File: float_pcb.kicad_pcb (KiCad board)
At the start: 4 copper layers, 64 x 64 mm, 77 parts, among them J1 Switch, J2 Conn_01x04, J3 USB_C, J4 Conn_01x03, J5 I2C, J6 Light, J7 Batt, J9 I2C, Q1 AO3400A, Q2 AO3400A, U1 TPSM863252, U2 TPSM863252, U3 USBLC6-2SC6, U4 ESP32-S3-WROOM-1, U5 USBLC6-4SC6, U6 USBLC6-4SC6

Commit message: More progress on V4
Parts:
- U4: value ESP32-S3-WROOM-1 -> ESP32-S3-WROOM-1U
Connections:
- net /VBUS renamed VBUS_USB
- net Net-(J3-D+-PadA6) renamed USBC_D+
- net Net-(J3-D--PadA7) renamed USBC_D-
- net Net-(U4-USB_D+) renamed ESP32_D+
- net Net-(U4-USB_D-) renamed ESP32_D-
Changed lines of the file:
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@@
 			)
 		)
-		(property "Value" "ESP32-S3-WROOM-1"
+		(property "Value" "ESP32-S3-WROOM-1U"
 			(at 0 2.46 0)
 			(unlocked yes)
@@
 			(size 1.5 0.9)
 			(layers "F.Cu" "F.Mask" "F.Paste")
-			(net "Net-(U4-USB_D-)")
+			(net "ESP32_D-")
 			(pinfunction "USB_D-_13")
 			(pintype "bidirectional")
@@
 			(size 1.5 0.9)
 			(layers "F.Cu" "F.Mask" "F.Paste")
-			(net "Net-(U4-USB_D+)")
+			(net "ESP32_D+")
 			(pinfunction "USB_D+_14")
 			(pintype "bidirectional")
@@
 			(layers "F.Cu" "F.Mask" "F.Paste")
 			(roundrect_rratio 0.25)
-			(net "/VBUS")
+			(net "VBUS_USB")
 			(pinfunction "VBUS_A4")
 			(pintype "passive")
@@
 			(layers "F.Cu" "F.Mask" "F.Paste")
 			(roundrect_rratio 0.25)
-			(net "Net-(J3-D+-PadA6)")
+			(net "USBC_D+")
 			(pinfunction "D+_A6")
 			(pintype "bidirectional")
@@
 			(layers "F.Cu" "F.Mask" "F.Paste")
 			(roundrect_rratio 0.25)
-			(net "Net-(J3-D--PadA7)")
+			(net "USBC_D-")
 			(pinfunction "D-_A7")
 			(pintype "bidirectional")
@@
 			(layers "F.Cu" "F.Mask" "F.Paste")
 			(roundrect_rratio 0.25)
-			(net "/VBUS")
+			(net "VBUS_USB")
 			(pinfunction "VBUS_A9")
 			(pintype "passive")
@@
 			(layers "F.Cu" "F.Mask" "F.Paste")
 			(roundrect_rratio 0.25)
-			(net "/VBUS")
+			(net "VBUS_USB")
 			(pinfunction "VBUS_B4")
 			(pintype "passive")
@@
 			(layers "F.Cu" "F.Mask" "F.Paste")
 			(roundrect_rratio 0.25)
-			(net "Net-(J3-D+-PadA6)")
+			(net "USBC_D+")
 			(pinfunction "D+_B6")
 			(pintype "bidirectional")
@@
 			(layers "F.Cu" "F.Mask" "F.Paste")
 			(roundrect_rratio 0.25)
-			(net "Net-(J3-D--PadA7)")
+			(net "USBC_D-")
 			(pinfunction "D-_B7")
 			(pintype "bidirectional")
@@
 			(layers "F.Cu" "F.Mask" "F.Paste")
 			(roundrect_rratio 0.25)
-			(net "/VBUS")
+			(net "VBUS_USB")
 			(pinfunction "VBUS_B9")
 			(pintype "passive")
@@
 			(layers "F.Cu" "F.Mask" "F.Paste")
 			(roundrect_rratio 0.25)
-			(net "Net-(U4-USB_D+)")
+			(net "ESP32_D+")
 			(pinfunction "I/O1_1")
 			(pintype "passive")
@@
 			(layers "F.Cu" "F.Mask" "F.Paste")
 			(roundrect_rratio 0.25)
-			(net "Net-(U4-USB_D-)")
+			(net "ESP32_D-")
 			(pinfunction "I/O2_3")
 			(pintype "passive")
@@
 			(layers "F.Cu" "F.Mask" "F.Paste")
 			(roundrect_rratio 0.25)
-			(net "Net-(J3-D--PadA7)")
+			(net "USBC_D-")
 			(pinfunction "I/O2_4")
 			(pintype "passive")
@@
 			(layers "F.Cu" "F.Mask" "F.Paste")
 			(roundrect_rratio 0.25)
-			(net "/VBUS")
+			(net "VBUS_USB")
 			(pinfunction "VBUS_5")
 			(pintype "passive")
@@
 			(layers "F.Cu" "F.Mask" "F.Paste")
 			(roundrect_rratio 0.25)
-			(net "Net-(J3-D+-PadA6)")
+			(net "USBC_D+")
 			(pinfunction "I/O1_6")
 			(pintype "passive")
@@
 	)
 	(segment
-		(start 142.43 116.925)
+		(start 142.075 116.925)
 		(end 139.5 116.925)
 		(width 0.2)
@@
 	)
 	(segment
-		(start 139.5 116.925)
-		(end 139.5 117.1375)
+		(start 144.055 114.35)
+		(end 144.055 114.945)
 		(width 0.2)
 		(layer "F.Cu")
@@
 	)
 	(segment
-		(start 144.055 115.3)
-		(end 142.43 116.925)
+		(start 139.5 116.925)
+		(end 139.5 117.1375)
 		(width 0.2)
 		(layer "F.Cu")
@@
 	)
 	(segment
-		(start 139.5 117.1375)
-		(end 136.1875 120.45)
+		(start 144.055 114.945)
+		(end 142.075 116.925)
 		(width 0.2)
 		(layer "F.Cu")
@@
 	)
 	(segment
-		(start 144.055 114.35)
-		(end 144.055 115.3)
+		(start 139.5 117.1375)
+		(end 136.1875 120.45)
 		(width 0.2)
 		(layer "F.Cu")
@@
 	)
 	(segment
-		(start 146.595 119.98)
+		(start 146.595 114.905)
 		(end 146.595 114.35)
 		(width 0.2)
@@
 	)
 	(segment
+		(start 145.325 116.175)
+		(end 146.595 114.905)
+		(width 0.2)
+		(layer "F.Cu")
+		(net "SCL1")
+	)
+	(segment
 		(start 138.5 130.5)
 		(end 138.5 129.575)
@@
 	(segment
 		(start 145.325 121.25)
-		(end 146.595 119.98)
+		(end 145.325 116.175)
 		(width 0.2)
 		(layer "F.Cu")
@@
 	)
 	(segment
-		(start 157.25 116.175)
-		(end 155.09 116.175)
-		(width 0.2)
-		(layer "F.Cu")
-		(net "BUZZER")
-	)
-	(segment
-		(start 154.215 115.3)
-		(end 154.215 114.35)
+		(start 155.425 116.175)
+		(end 154.215 114.965)
 		(width 0.2)
 		(layer "F.Cu")
@@
 	)
 	(segment
-		(start 155.09 116.175)
-		(end 154.215 115.3)
+		(start 157.25 116.175)
+		(end 155.425 116.175)
 		(width 0.2)
 		(layer "F.Cu")
@@
 	)
 	(segment
-		(start 157.5 80.675)
-		(end 157.5 79.0575)
-		(width 0.2)
-		(layer "F.Cu")
-		(net "Net-(D1-A)")
-	)
-	(segment
-		(start 138.8 111.83)
-		(end 138.314927 111.344927)
+		(start 154.215 114.965)
+		(end 154.215 114.35)
 		(width 0.2)
 		(layer "F.Cu")
-		(net "Net-(U4-USB_D-)")
+		(net "BUZZER")
 	)
 	(segment
-		(start 138.314927 110.698628)
-		(end 131.666299 104.05)
+		(start 157.5 80.675)
+		(end 157.5 79.0575)
 		(width 0.2)
 		(layer "F.Cu")
-		(net "Net-(U4-USB_D-)")
+		(net "Net-(D1-A)")
 	)
 	(segment
-		(start 131.666299 104.05)
-		(end 130.3875 104.05)
+		(start 131.448529 104.05)
+		(end 139.228529 111.83)
 		(width 0.2)
 		(layer "F.Cu")
-		(net "Net-(U4-USB_D-)")
+		(net "ESP32_D-")
 	)
 	(segment
-		(start 138.314927 111.344927)
-		(end 138.314927 110.698628)
+		(start 139.228529 111.83)
+		(end 139.75 111.83)
 		(width 0.2)
 		(layer "F.Cu")
-		(net "Net-(U4-USB_D-)")
+		(net "ESP32_D-")
 	)
 	(segment
-		(start 139.75 111.83)
-		(end 138.8 111.83)
+		(start 130.3875 104.05)
+		(end 131.448529 104.05)
 		(width 0.2)
 		(layer "F.Cu")
-		(net "Net-(U4-USB_D-)")
+		(net "ESP32_D-")
 	)
 	(segment
@@
 		(width 0.2)
 		(layer "F.Cu")
-		(net "Net-(U4-USB_D+)")
+		(net "ESP32_D+")
 	)
 	(segment
@@
 		(width 0.2)
 		(layer "F.Cu")
-		(net "Net-(U4-USB_D+)")
+		(net "ESP32_D+")
 	)
 	(segment
@@
 		(width 0.2)
 		(layer "F.Cu")
-		(net "Net-(U4-USB_D+)")
+		(net "ESP32_D+")
 	)
 	(segment
@@
 		(width 0.2)
 		(layer "F.Cu")
-		(net "/VBUS")
+		(net "VBUS_USB")
 	)
 	(segment
@@
 		(width 0.2)
 		(layer "F.Cu")
-		(net "/VBUS")
+		(net "VBUS_USB")
 	)
 	(segment
@@
 		(width 0.2)
 		(layer "F.Cu")
-		(net "/VBUS")
+		(net "VBUS_USB")
 	)
 	(segment
@@
 		(width 0.2)
 		(layer "F.Cu")
-		(net "/VBUS")
+		(net "VBUS_USB")
 	)
 	(segment
@@
 		(width 0.2)
 		(layer "F.Cu")
-		(net "/VBUS")
+		(net "VBUS_USB")
 	)
 	(via
@@
 		(drill 0.3)
 		(layers "F.Cu" "B.Cu")
-		(net "/VBUS")
+		(net "VBUS_USB")
 	)
 	(via
@@
 		(drill 0.3)
 		(layers "F.Cu" "B.Cu")
-		(net "/VBUS")
+		(net "VBUS_USB")
 	)
 	(via
@@
 		(drill 0.3)
 		(layers "F.Cu" "B.Cu")
-		(net "/VBUS")
+		(net "VBUS_USB")
 	)
 	(segment
@@
 		(width 0.2)
 		(layer "B.Cu")
-		(net "/VBUS")
+		(net "VBUS_USB")
 	)
 	(segment
@@
 		(width 0.2)
 		(layer "B.Cu")
-		(net "/VBUS")
+		(net "VBUS_USB")
 	)
 	(segment
@@
 		(width 0.2)
 		(layer "B.Cu")
-		(net "/VBUS")
+		(net "VBUS_USB")
 	)
 	(segment
@@
 		(width 0.2)
 		(layer "B.Cu")
-		(net "/VBUS")
+		(net "VBUS_USB")
 	)
 	(segment
@@
 		(width 0.2)
 		(layer "F.Cu")
-		(net "Net-(J3-D+-PadA6)")
+		(net "USBC_D+")
 	)
 	(segment
@@
 		(width 0.2)
 		(layer "F.Cu")
-		(net "Net-(J3-D+-PadA6)")
+		(net "USBC_D+")
 	)
 	(segment
@@
 		(width 0.2)
 		(layer "F.Cu")
-		(net "Net-(J3-D+-PadA6)")
+		(net "USBC_D+")
 	)
 	(segment
@@
 		(width 0.2)
 		(layer "F.Cu")
-		(net "Net-(J3-D+-PadA6)")
+		(net "USBC_D+")
 	)
 	(segment
@@
 		(width 0.2)
 		(layer "F.Cu")
-		(net "Net-(J3-D+-PadA6)")
+		(net "USBC_D+")
 	)
 	(segment
@@
 		(width 0.2)
 		(layer "F.Cu")
-		(net "Net-(J3-D+-PadA6)")
+		(net "USBC_D+")
 	)
 	(segment
@@
 		(width 0.2)
 		(layer "F.Cu")
-		(net "Net-(J3-D+-PadA6)")
+		(net "USBC_D+")
 	)
 	(segment
@@
 		(width 0.2)
 		(layer "F.Cu")
-		(net "Net-(J3-D--PadA7)")
+		(net "USBC_D-")
 	)
 	(segment
@@
 		(width 0.2)
 		(layer "F.Cu")
-		(net "Net-(J3-D--PadA7)")
+		(net "USBC_D-")
 	)
 	(segment
@@
 		(width 0.2)
 		(layer "F.Cu")
-		(net "Net-(J3-D--PadA7)")
+		(net "USBC_D-")
 	)
 	(segment
@@
 		(width 0.2)
 		(layer "F.Cu")
-		(net "Net-(J3-D--PadA7)")
+		(net "USBC_D-")
 	)
 	(segment
@@
 		(width 0.2)
 		(layer "F.Cu")
-		(net "Net-(J3-D--PadA7)")
+		(net "USBC_D-")
 	)
 	(segment
@@
 		(width 0.2)
 		(layer "F.Cu")
-		(net "Net-(J3-D--PadA7)")
+		(net "USBC_D-")
 	)
 	(segment
@@
 		(width 0.2)
 		(layer "F.Cu")
-		(net "Net-(J3-D--PadA7)")
+		(net "USBC_D-")
 	)
 	(zone

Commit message: Using open source fonts
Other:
- board text added: "9V MAX"
- board text added: "EVAN KIM '27"
- board text added: "REV A (6/26)"
- board text removed: "Evan Kim '27"
- board text removed: "REV A"

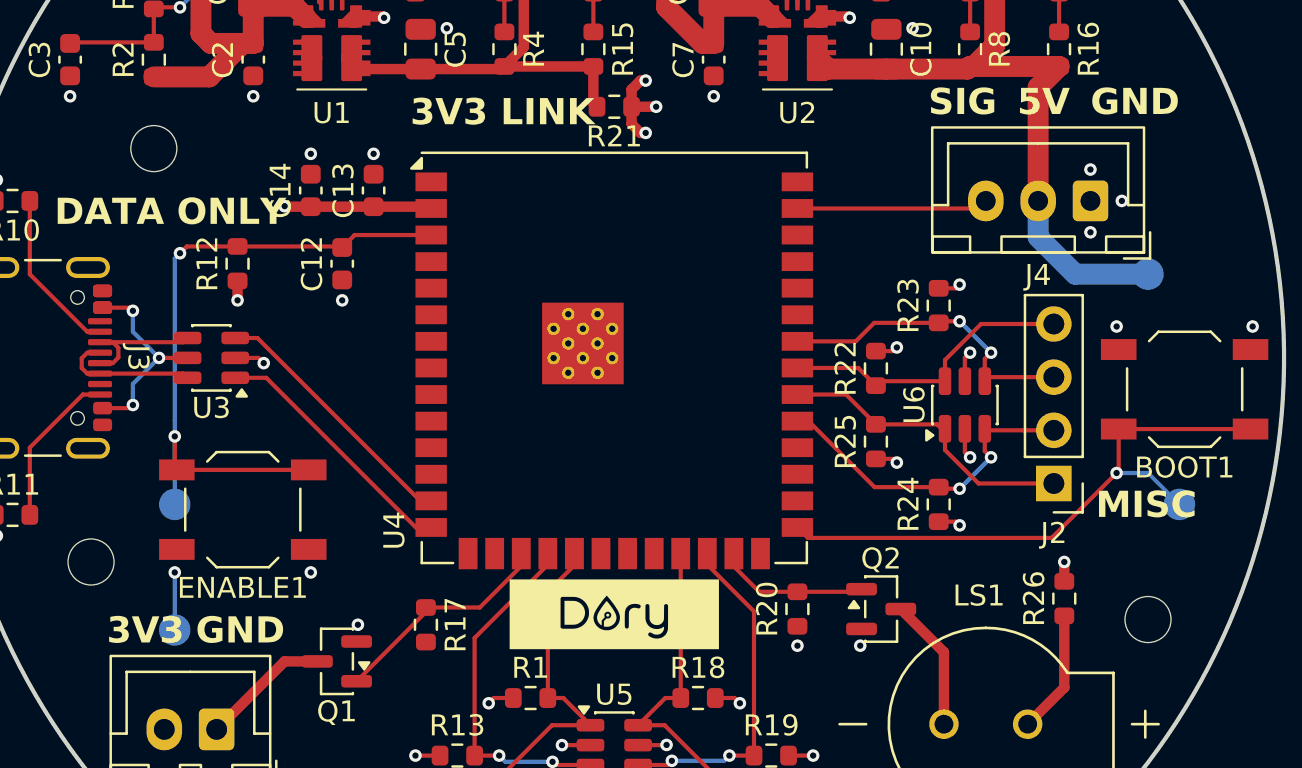
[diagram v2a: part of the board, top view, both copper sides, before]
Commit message: Change hole placement
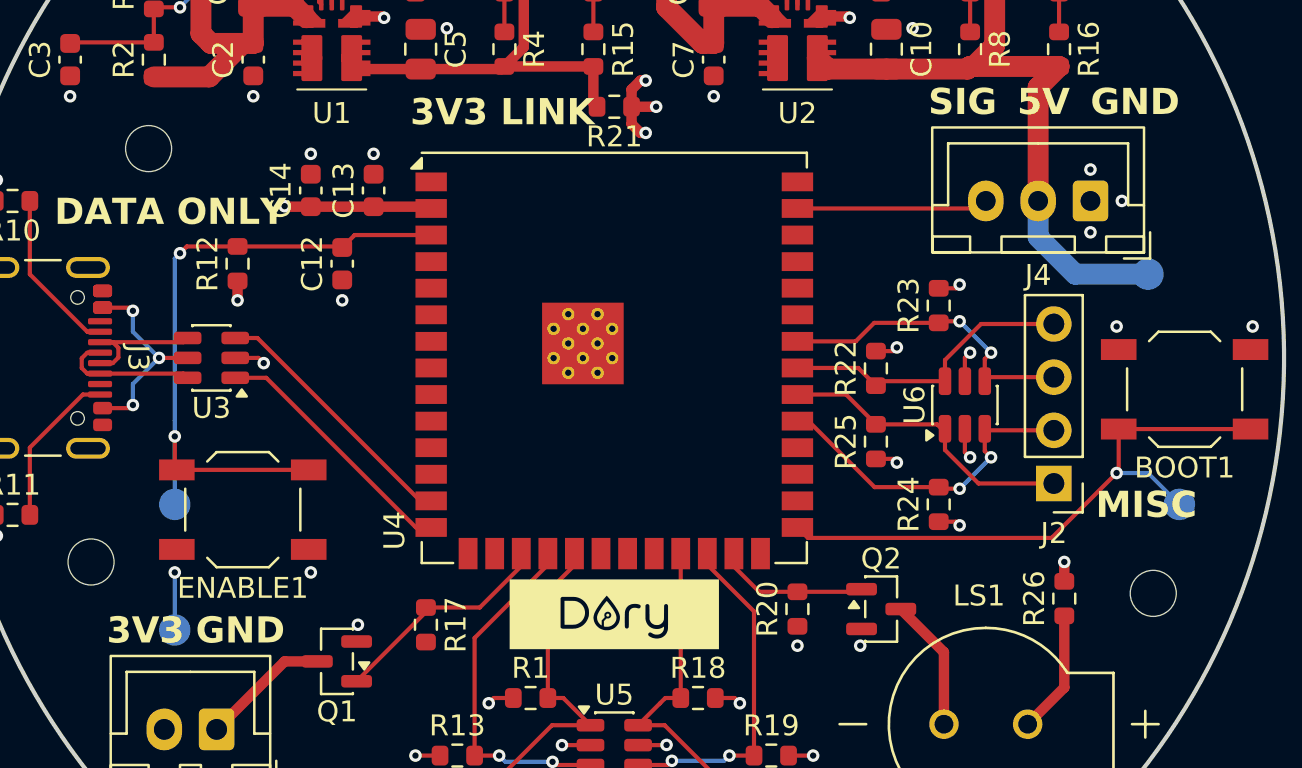
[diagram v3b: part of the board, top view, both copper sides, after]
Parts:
- moved H2 1.27 mm to (174.2, 116.2)
- moved H1 0.25 mm to (126.2, 95.0)
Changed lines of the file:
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@@
 	(footprint "MountingHole:MountingHole_2.2mm_M2"
 		(layer "F.Cu")
-		(at 126.5 95)
+		(at 126.25 95)
 		(descr "Mounting Hole 2.2mm, M2, no annular, generated by kicad-footprint-generator mountinghole.py")
 		(tags "mountinghole M2")
@@
 	(footprint "MountingHole:MountingHole_2.2mm_M2"
 		(layer "F.Cu")
-		(at 174 117.5)
+		(at 174.25 116.25)
 		(descr "Mounting Hole 2.2mm, M2, no annular, generated by kicad-footprint-generator mountinghole.py")
 		(tags "mountinghole M2")

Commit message: V4
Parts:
- removed Q2: AO3400A, Package_TO_SOT_SMD:SOT-23
- removed R26: TBD, Resistor_SMD:R_0603_1608Metric
- removed U3: USBLC6-2SC6, Package_TO_SOT_SMD:SOT-23-6
- removed U5, U6: USBLC6-4SC6, Package_TO_SOT_SMD:SOT-23-6
- added D4: ESDS314, Package_TO_SOT_SMD:SOT-23-5, F.Cu at (129.5, 105.0)
- added D5: ESDS314, Package_TO_SOT_SMD:SOT-23-5, F.Cu at (165.2, 107.2)
- added D6: ESDS314, Package_TO_SOT_SMD:SOT-23-5, F.Cu at (148.5, 123.5)
- added H4: MH, MountingHole:MountingHole_2.2mm_M2, F.Cu at (176.7, 97.2)
- J2: value Conn_01x04 -> Conn_01x05; footprint Connector_PinHeader_2.54mm:PinHeader_1x04_P2.54mm_Vertical -> Connector_PinHeader_2.54mm:PinHeader_1x05_P2.54mm_Vertical
- LS1: value AT-1127-ST-2-R -> CPT-9019A-SMT-TR; footprint buzzer:XDCR_AT-1127-ST-2-R -> buzzer:CPT-9019A_CUD
- R20: value 10k -> 1k
- TP7: value SDA2 -> SDA1
- moved H2 14.4 mm to (166.0, 128.0)
- moved J2 8.00 mm to (169.5, 103.0), turned to 0 degrees
- moved R20 3.58 mm to (158.8, 120.2), turned to 0 degrees
- moved H1 3.01 mm to (129.2, 95.2)
- moved LS1 2.46 mm to (167.2, 120.2)
- moved R12 1.75 mm to (132.2, 100.5)
- moved C12 1.00 mm to (136.5, 100.5)
- moved R17 0.25 mm to (139.5, 117.5)
- renumbered R25 to R22, R22 to R25
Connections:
- net VBUS_USB renamed /USB_VBUS
- R17 pad 1: LIGHT -> GND
- R17 pad 2: GND -> LIGHT
- R20 pad 1: GND -> BUZZER
- R20 pad 2: BUZZER -> Net-(LS1-Pad1)
- R22 pad 2: MISC1 -> MISC4
- R23 pad 1: MISC3 -> MISC2
- R24 pad 2: MISC2 -> MISC3
- R25 pad 1: MISC4 -> MISC1
- U4 pad 13: ESP32_D- -> USBC_D-
- U4 pad 14: ESP32_D+ -> USBC_D+
- U4 pad 31: MISC2 -> MISC3
- U4 pad 32: MISC1 -> MISC4
- U4 pad 33: MISC4 -> MISC1
- U4 pad 34: MISC3 -> MISC2
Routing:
- net USBC_D-: track 6.70 -> 21.6 mm
- net USBC_D+: track 6.70 -> 21.3 mm
- net ESP32_D-: track 12.6 -> 0.00 mm
- net ESP32_D+: track 12.3 -> 0.00 mm
- net Net-(Q2-D): track 6.35 -> 0.00 mm
- net Net-(LS1-PadP): track 5.90 -> 0.00 mm
- net +3V3: track 30.0 -> 26.2 mm, vias 16 -> 13
- net Net-(LS1-Pad1): track 0.00 -> 3.42 mm
- net /USB_VBUS: track 9.92 -> 6.93 mm, vias 3 -> 2
- net Net-(U4-EN): track 32.4 -> 30.8 mm
- net MISC3: track 14.9 -> 16.0 mm
- net MISC2: track 16.0 -> 14.9 mm
- net GND: track 9.77 -> 10.8 mm, vias 35 -> 37
- net Net-(U4-IO0): track 28.8 -> 28.4 mm, vias 1 -> 2

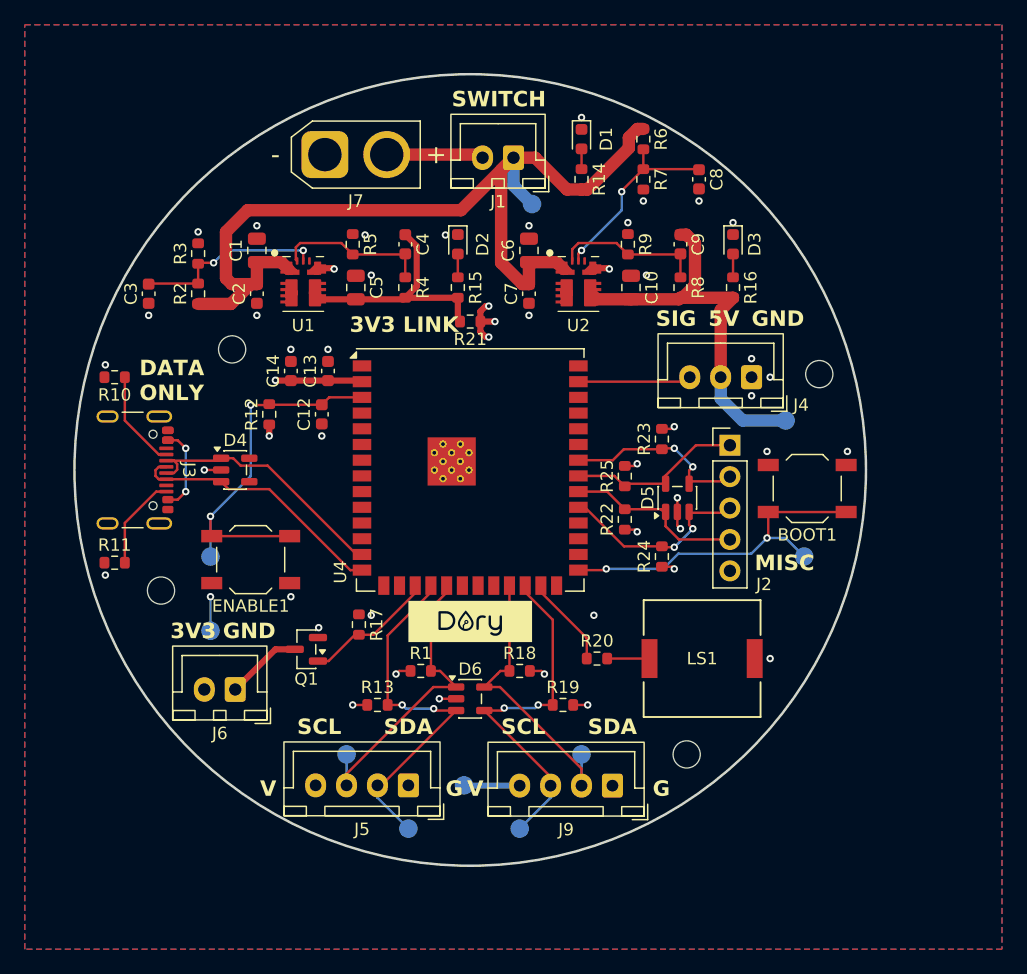
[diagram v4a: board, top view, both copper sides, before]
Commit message: Starting V5: new 33uf new servo cap, ADC and voltage dividor
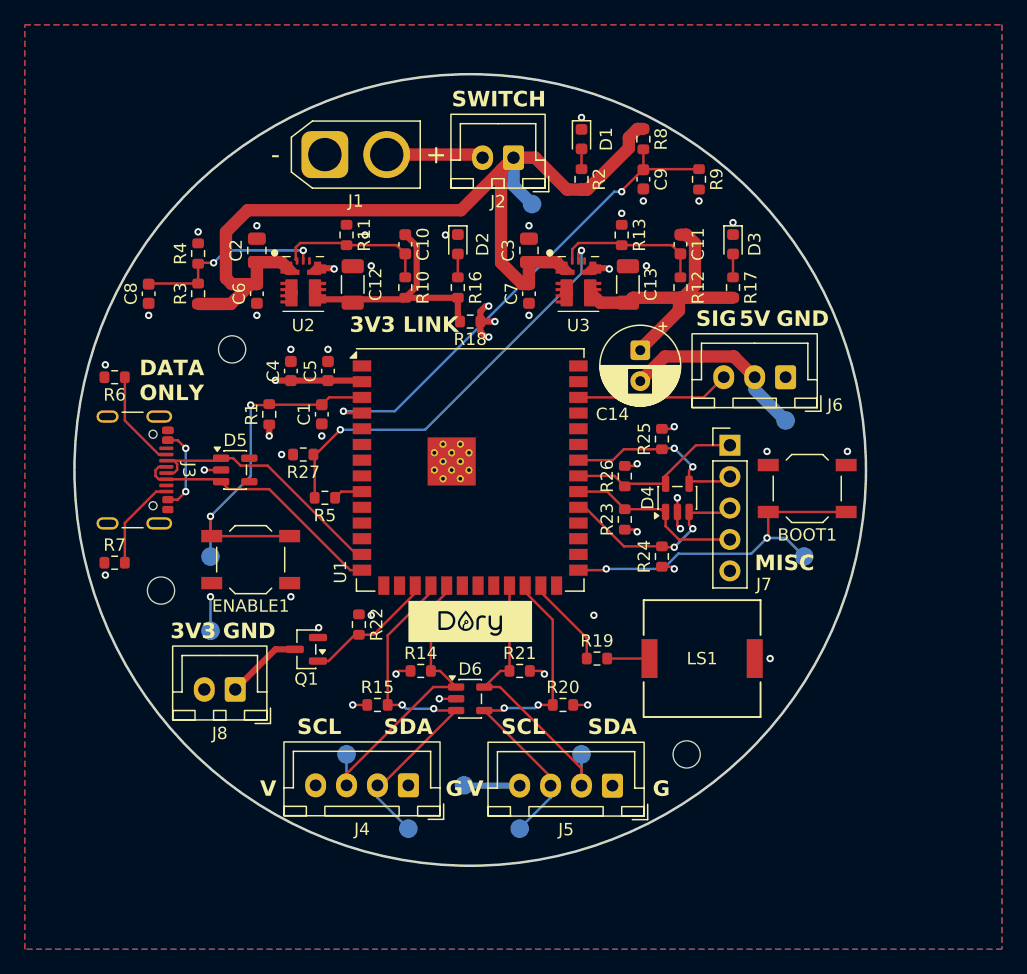
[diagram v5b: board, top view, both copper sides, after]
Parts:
- removed the C8 at (167.0, 81.5)
- removed H4: MH, MountingHole:MountingHole_2.2mm_M2
- removed the R6 at (162.5, 78.2)
- removed the R7 at (162.5, 81.5)
- removed the TP1 at (174.0, 101.0)
- added C14: 470uF, Capacitor_THT:CP_Radial_D6.3mm_P2.50mm, F.Cu at (162.2, 95.3)
- added C9: 100n, Capacitor_SMD:C_0603_1608Metric, F.Cu at (162.5, 81.5)
- added R27: 100k, Resistor_SMD:R_0603_1608Metric, F.Cu at (135.0, 103.8)
- added R5: 10k, Resistor_SMD:R_0603_1608Metric, F.Cu at (136.8, 107.2)
- added R8: 220k, Resistor_SMD:R_0603_1608Metric, F.Cu at (162.5, 78.2)
- added R9: 100k, Resistor_SMD:R_0603_1608Metric, F.Cu at (167.0, 81.5)
- added TP9: 5V, TestPoint:TestPoint_Pad_D1.5mm, B.Cu at (174.0, 101.0)
- C12: renamed from C5; footprint Capacitor_SMD:C_0805_2012Metric -> Capacitor_SMD:C_1206_3216Metric
- C13: renamed from C10; footprint Capacitor_SMD:C_0805_2012Metric -> Capacitor_SMD:C_1206_3216Metric
- moved J6 2.75 mm to (174.0, 97.5)
- moved R11 0.90 mm to (138.5, 86.0)
- moved R13 0.90 mm to (160.8, 86.0)
- moved C12 0.35 mm to (139.0, 90.0)
- moved C13 0.35 mm to (161.2, 90.0)
- renumbered C12 to C1, C4 to C10, C9 to C11, C1 to C2, C6 to C3, C14 to C4, C13 to C5, C2 to C6, C3 to C8, D5 to D4, D4 to D5, H3 to H2, H2 to H3, J7 to J1, J1 to J2, J5 to J4, J9 to J5, J4 to J6, J2 to J7, J6 to J8, R12 to R1, R4 to R10, R5 to R11, R8 to R12, R9 to R13, R1 to R14, R13 to R15, R15 to R16, R16 to R17, R21 to R18, R20 to R19, R14 to R2, R19 to R20, R18 to R21, R17 to R22, R22 to R23, R23 to R25, R25 to R26, R2 to R3, R3 to R4, R10 to R6, R11 to R7, TP3 to TP1, TP2 to TP10, TP4 to TP2, TP10 to TP3, TP9 to TP4, TP8 to TP5, TP7 to TP6, TP5 to TP7, TP6 to TP8, U4 to U1, U1 to U2, U2 to U3
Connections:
- C11 pad 1: Net-(J4-Pin_2) -> Net-(U3-VOUT)
- C13 pad 2: Net-(J4-Pin_2) -> Net-(U3-VOUT)
- J6 pad 2: Net-(J4-Pin_2) -> Net-(J6-Pin_2)
- R12 pad 2: Net-(J4-Pin_2) -> Net-(U3-VOUT)
- R17 pad 2: Net-(J4-Pin_2) -> Net-(U3-VOUT)
- U1 pad 38: unconnected-(U4-IO2-Pad38) -> SERVO
- U1 pad 39: SERVO -> unconnected-(U1-IO1-Pad39)
- U1 pad 4: unconnected-(U4-IO4-Pad4) -> BATT_SENSE
- U1 pad 9: unconnected-(U4-IO16-Pad9) -> EN_5V
- U3 pad 3: Net-(J4-Pin_2) -> Net-(U3-VOUT)
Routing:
- net BATT_SENSE: track 0.00 -> 40.1 mm, vias 0 -> 2
- net Net-(J4-Pin_2): track 32.8 -> 0.00 mm
- net Net-(U3-VOUT): track 0.00 -> 24.1 mm
- net Net-(U3-EN): track 15.7 -> 34.1 mm
- net Net-(J6-Pin_2): track 0.00 -> 15.3 mm
- net SERVO: track 9.15 -> 12.4 mm
- net EN_5V: track 0.00 -> 2.38 mm
- net GND: vias 37 -> 35
